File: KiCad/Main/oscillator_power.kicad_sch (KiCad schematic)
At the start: 13 parts, among them U5 TL074, U6 TL074, U7 TL074

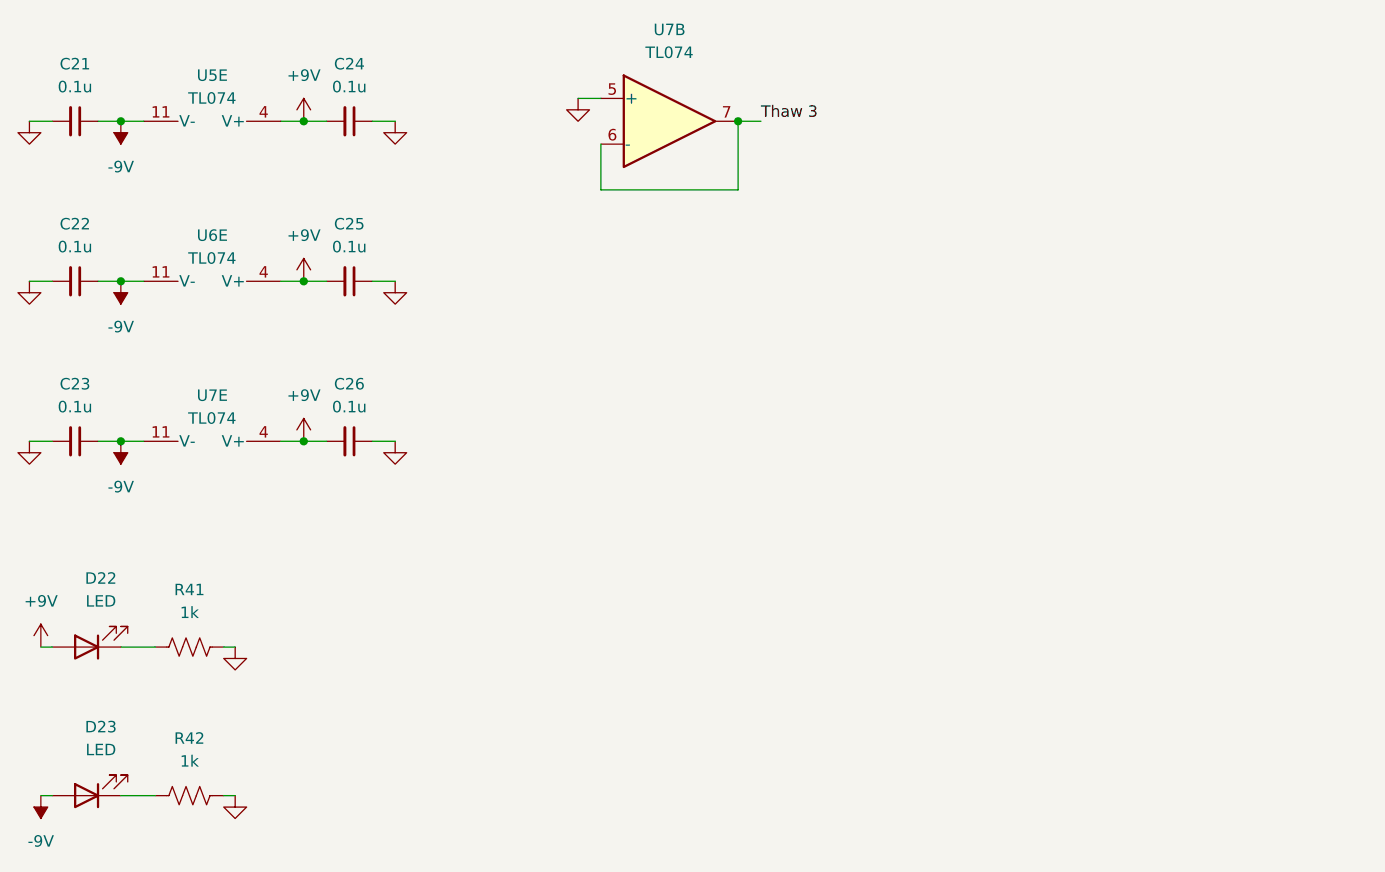
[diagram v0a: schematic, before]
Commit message: merged project into one combined board (excluding the buttons)
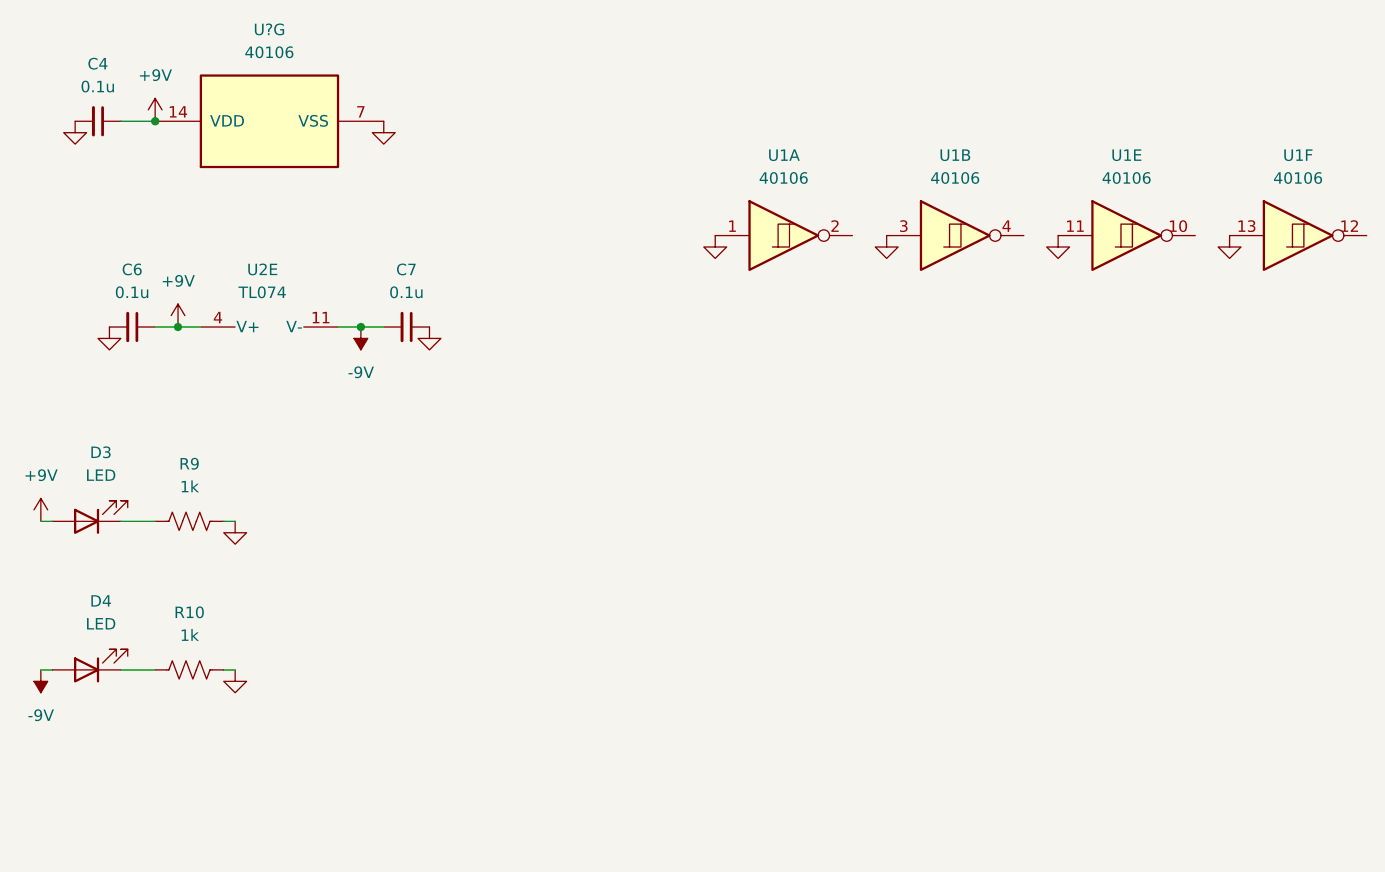
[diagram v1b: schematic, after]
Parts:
- removed C21, C22, C23, C24, C25, C26: 0.1u, Capacitor_SMD:C_0805_2012Metric, symbol Device:C_Small
- removed D22, D23: LED, LED_THT:LED_D5.0mm, symbol Device:LED
- removed R41, R42: 1k, Resistor_SMD:R_0805_2012Metric, symbol Device:R_US
- removed U5, U6, U7: TL074, Package_DIP:DIP-14_W7.62mm, symbol Amplifier_Operational:TL074
- added C4, C6, C7: 0.1u, Capacitor_SMD:C_0805_2012Metric, symbol Device:C_Small
- added D3, D4: LED, LED_THT:LED_D5.0mm, symbol Device:LED
- added R10, R9: 1k, Resistor_SMD:R_0805_2012Metric, symbol Device:R_US
- added U1, U?: 40106, Package_DIP:DIP-14_W7.62mm, symbol 4xxx:40106
- added U2: TL074, Package_DIP:DIP-14_W7.62mm, symbol Amplifier_Operational:TL074
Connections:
- net +9V: now also C4.1, C6.1, D3.2 (A), U2.4 (V+), U?.14 (VDD)
- net -9V: now also C7.2, D4.2 (A), U2.11 (V-)
- net GND: now also C4.2, C6.2, C7.1, R10.2, R9.2, U1.1, U1.11, U1.13, U1.3, U?.7 (VSS)
- new net: D3.1 (K), R9.1
- new net: D4.1 (K), R10.1
